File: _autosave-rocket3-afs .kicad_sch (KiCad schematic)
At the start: 98 parts, among them IC1 ISL85005AFRZ-T7A, J1 ARMING_PLUG, J2 POWER, J3 E-MATCH_DROGUE, J4 SWD, J5 E-MATCH_RECOVERY, M5 MG90S, M6 MG90S, M7 MG90S, M8 MG90s, Q1 Q_NMOS_GSD, Q2 Q_NMOS_GSD, Q3 Q_NMOS_GSD, Q4 Q_NMOS_GSD, Q6 BC547, U2 MP1584EN-LF-Z, U8 USBLC6-2SC6, U9 MMC5983MA, Y1 16MHz

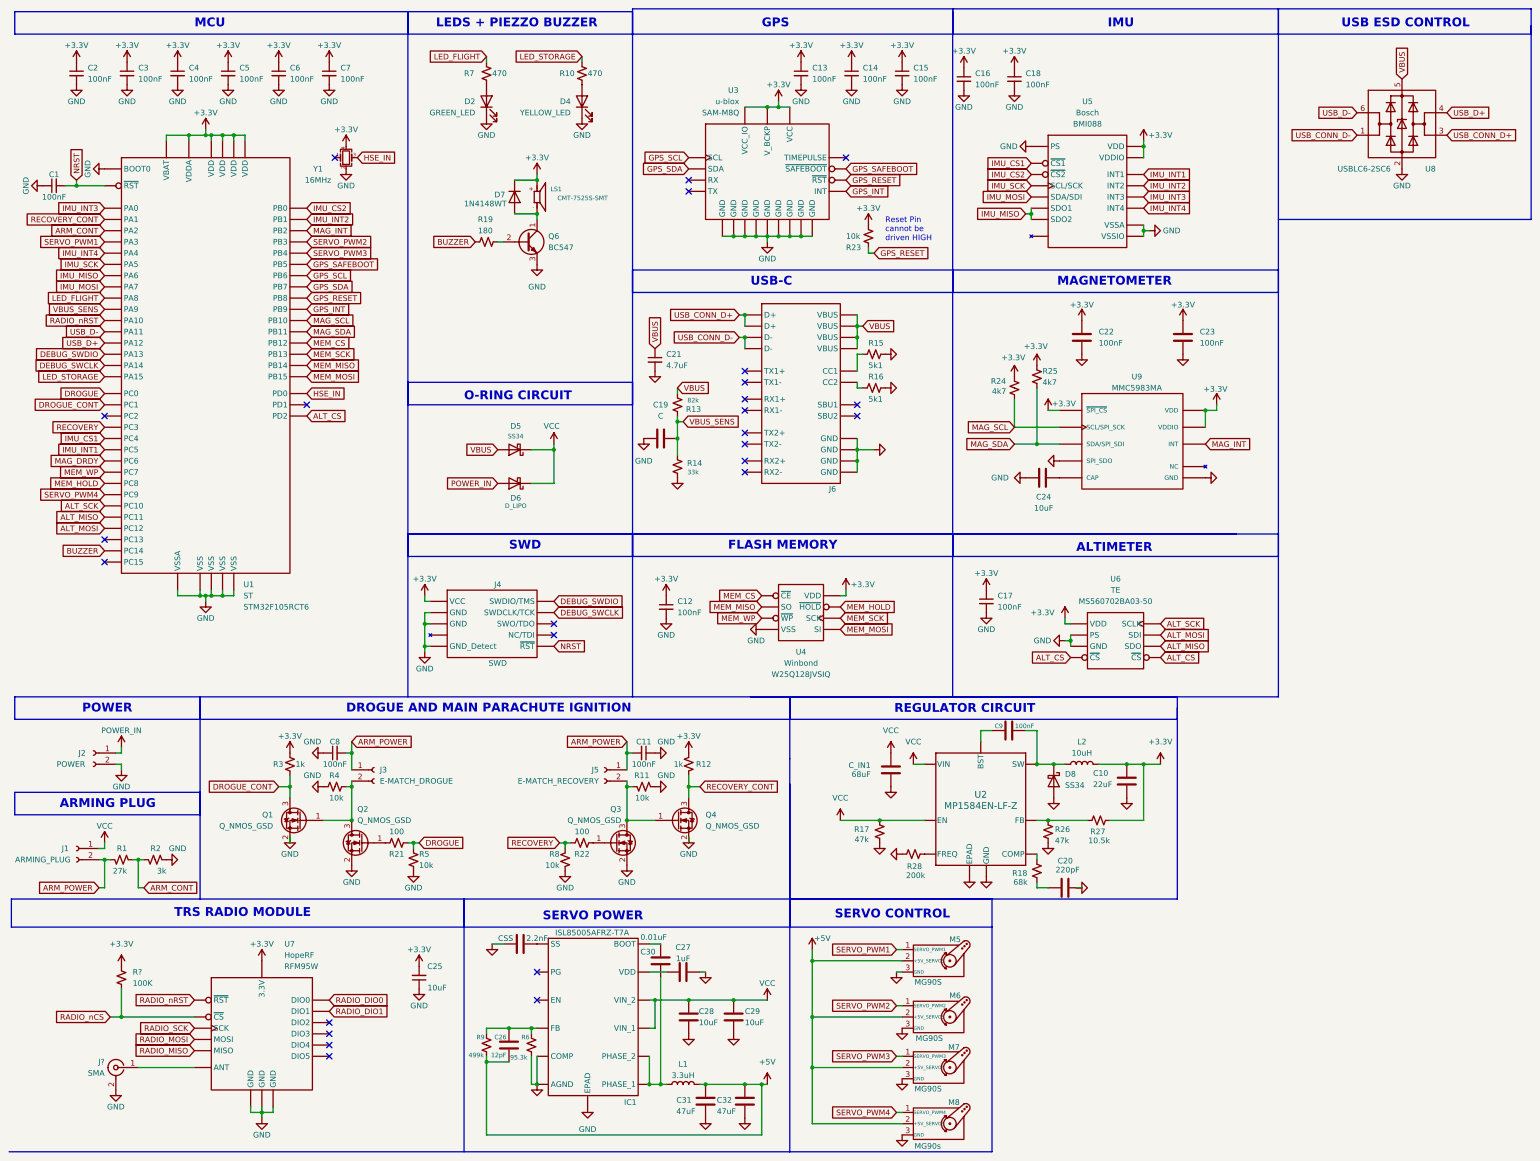
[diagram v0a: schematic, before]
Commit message: servo regulator circuit added
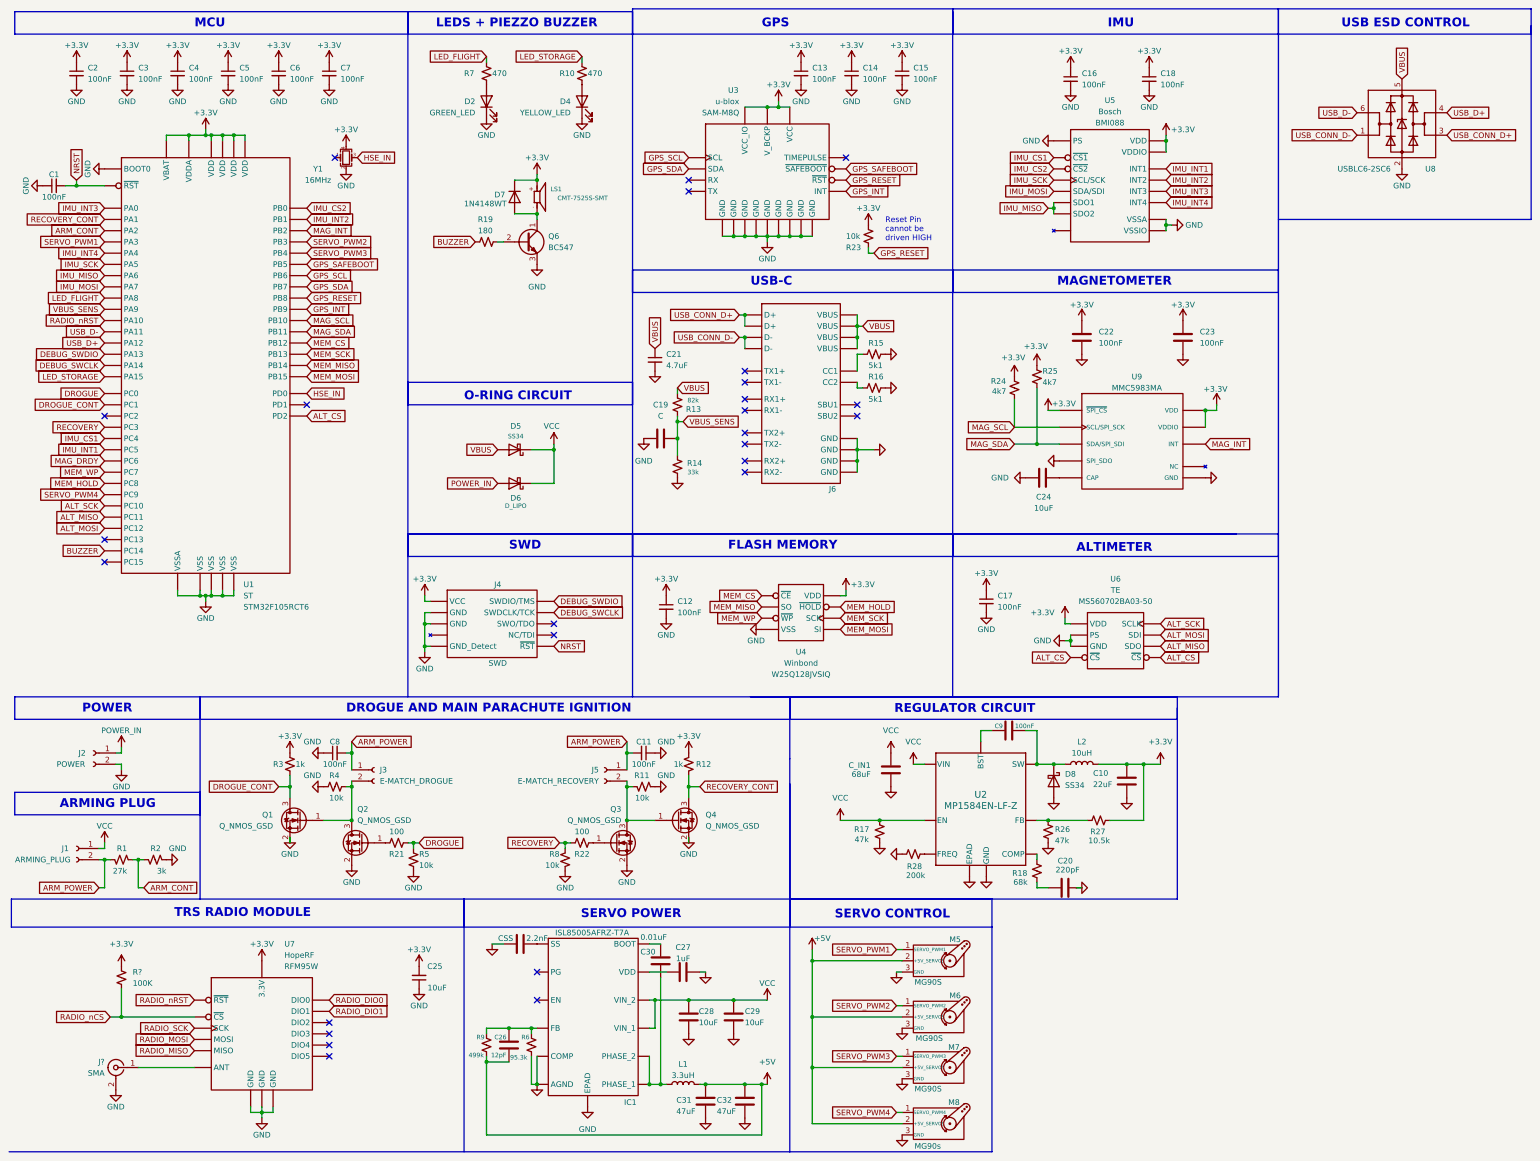
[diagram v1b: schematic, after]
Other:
- moved on the sheet: C16, C18, U5
